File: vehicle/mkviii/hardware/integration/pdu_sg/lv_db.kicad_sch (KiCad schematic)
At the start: 32 parts, among them U3 ACS37010LLZATR-030B5, U4 ACS37010LLZATR-030B5, U5 ACS37010LLZATR-030B5, U6 ACS37010LLZATR-030B5, U7 ACS37010LLZATR-030B5, U8 ACS37010LLZATR-030B5

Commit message: lv power distribution + rs232
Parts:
- removed R4: R_200_0.1W, OEM:R_0603_1608Metric, symbol OEM:R_200_0.1W_0603
- added R14: R_20k_2W, OEM:R_2512_6332Metric, symbol OEM:R_20k_2W_2512
- added R15: R_12k_0.1W, OEM:R_0603_1608Metric, symbol OEM:R_12k_0.1W_0603
- added R4: R_499, OEM:R_0603_1608Metric, symbol OEM:R_499_0.1W_0603
- added TP6: TP_SMD, OEM:TP_Hook_SMD, symbol OEM_mkvii:TP_Hook_SMD
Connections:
- net GND: now also R15.2, TP6.1
- net at F1.2, F2.2, F3.1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: now also R14.1, R4.1
- net at D4.2 (A): now also R4.2
- net 12V_PDU: now reaches U3.4 (IP-)
- new net V_SENSE: R14.2, R15.1
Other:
- sheet 3V3_buck renamed 3V3 buck
- added sheet 5V buck (buck_can.kicad_sch)
- sheet 3V3 buck ports: added 3v3_buck_vin, 3v3_buck_vout; removed none
- moved on the sheet: C10, C11, C12, C13, C14, C15, D4, D5, D6, D7, D8, D9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

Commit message: fix symbols after changing library
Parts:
- D4, D5: footprint OEM:D_0805_2012Metric -> Diode_SMD:D_0805_2012Metric
- D9: footprint (none) -> Resistor_SMD:R_2512_6332Metric
- R14: footprint OEM:R_2512_6332Metric -> Resistor_SMD:R_2512_6332Metric
- R15, R4, R5, R6, R7, R8, R9: footprint OEM:R_0603_1608Metric -> Resistor_SMD:R_0603_1608Metric
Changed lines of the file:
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@@
 			)
 		)
-		(property "Footprint" "OEM:R_2512_6332Metric"
+		(property "Footprint" "Resistor_SMD:R_2512_6332Metric"
 			(at 55.372 111.76 90)
 			(hide yes)
@@
 			)
 		)
-		(property "Footprint" "OEM:R_0603_1608Metric"
+		(property "Footprint" "Resistor_SMD:R_0603_1608Metric"
 			(at 33.782 111.76 90)
 			(hide yes)
@@
 			)
 		)
-		(property "Footprint" ""
+		(property "Footprint" "Resistor_SMD:R_2512_6332Metric"
 			(at 171.45 149.86 0)
 			(hide yes)
@@
 			)
 		)
-		(property "Footprint" "OEM:R_0603_1608Metric"
+		(property "Footprint" "Resistor_SMD:R_0603_1608Metric"
 			(at 55.372 124.46 90)
 			(hide yes)
@@
 			)
 		)
-		(property "Footprint" "OEM:R_0603_1608Metric"
+		(property "Footprint" "Resistor_SMD:R_0603_1608Metric"
 			(at 169.672 100.33 90)
 			(hide yes)
@@
 			)
 		)
-		(property "Footprint" "OEM:R_0603_1608Metric"
+		(property "Footprint" "Resistor_SMD:R_0603_1608Metric"
 			(at 169.672 142.24 90)
 			(hide yes)
@@
 			)
 		)
-		(property "Footprint" "OEM:R_0603_1608Metric"
+		(property "Footprint" "Resistor_SMD:R_0603_1608Metric"
 			(at 101.092 68.58 90)
 			(hide yes)
@@
 			)
 		)
-		(property "Footprint" "OEM:D_0805_2012Metric"
+		(property "Footprint" "Diode_SMD:D_0805_2012Metric"
 			(at 35.56 119.38 0)
 			(hide yes)
@@
 			)
 		)
-		(property "Footprint" "OEM:R_0603_1608Metric"
+		(property "Footprint" "Resistor_SMD:R_0603_1608Metric"
 			(at 173.228 52.07 90)
 			(hide yes)
@@
 			)
 		)
-		(property "Footprint" "OEM:R_0603_1608Metric"
+		(property "Footprint" "Resistor_SMD:R_0603_1608Metric"
 			(at 101.092 113.03 90)
 			(hide yes)
@@
 			)
 		)
-		(property "Footprint" "OEM:D_0805_2012Metric"
+		(property "Footprint" "Diode_SMD:D_0805_2012Metric"
 			(at 102.87 76.2 0)
 			(hide yes)

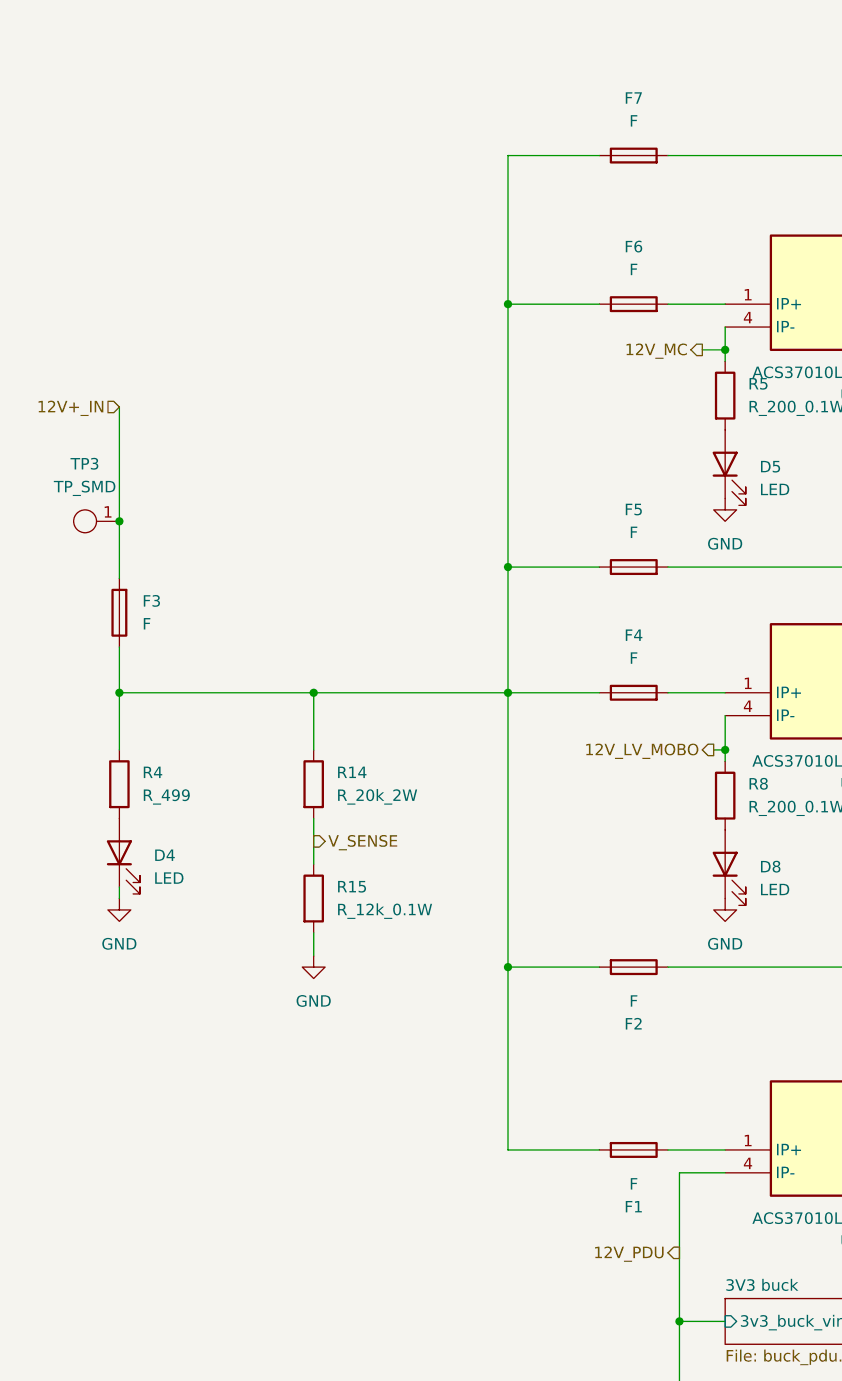
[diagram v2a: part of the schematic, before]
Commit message: fix footprints
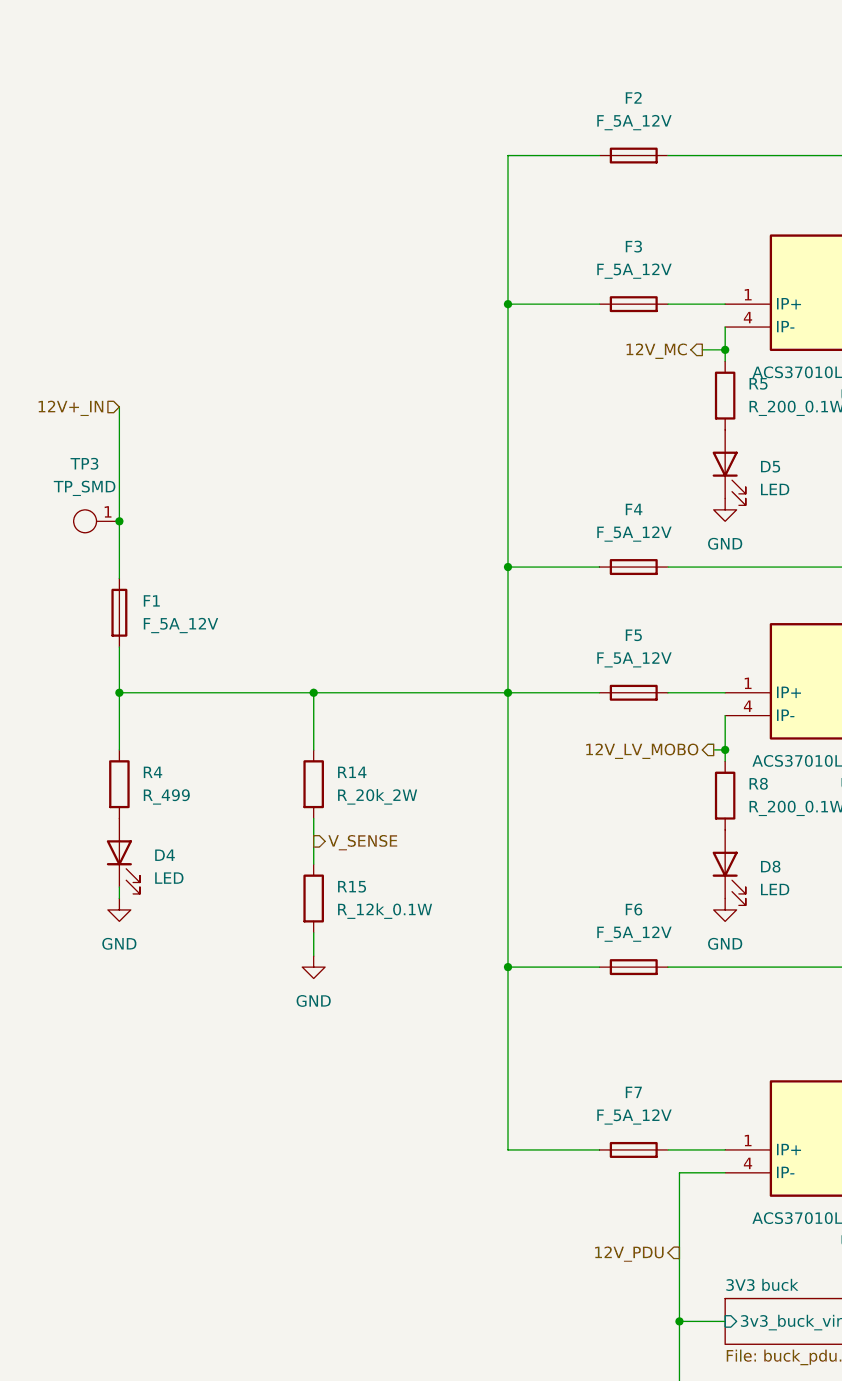
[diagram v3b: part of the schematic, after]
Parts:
- removed F1: F, OEM:U_Current-Sensor_ACS37010LLZATR-030B5_SOIC-6, symbol OEM:F
- removed F2, F3, F4, F5, F6, F7: F, symbol OEM:F
- added F1, F2, F3, F4, F5, F6, F7: F_5A_12V, Fuse:Fuse_1210_3225Metric, symbol OEM:F_5A_12V_1210
- C10, C11, C12, C13, C14, C15: footprint OEM:C_0603_1608Metric -> Capacitor_SMD:C_0603_1608Metric
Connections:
- net 12V+_IN: now also F1.1
- net at U8.1 (IP+): now also F2.2
- net at R14.1, R4.1: now also F1.2, F2.1, F3.1, F4.1, F5.1, F6.1, F7.1
- net at U6.1 (IP+): now also F4.2
- net at U3.1 (IP+): now also F7.2
- net at U4.1 (IP+): now also F6.2
- net at U5.1 (IP+): now also F5.2
- net at U7.1 (IP+): now also F3.2
